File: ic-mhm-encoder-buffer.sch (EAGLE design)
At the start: 35 parts, among them IC1 LS7183-SOIC, J1 2023960907, J2 2023960607, M1 BSS670S2LH6327XTSA1, SW1 CS-4-13NTA, U1 24LC16BT-I/MC, U2 D5V0F4U6S-7, U3 D5V0F4U6S-7, U4 D5V0F4U6S-7

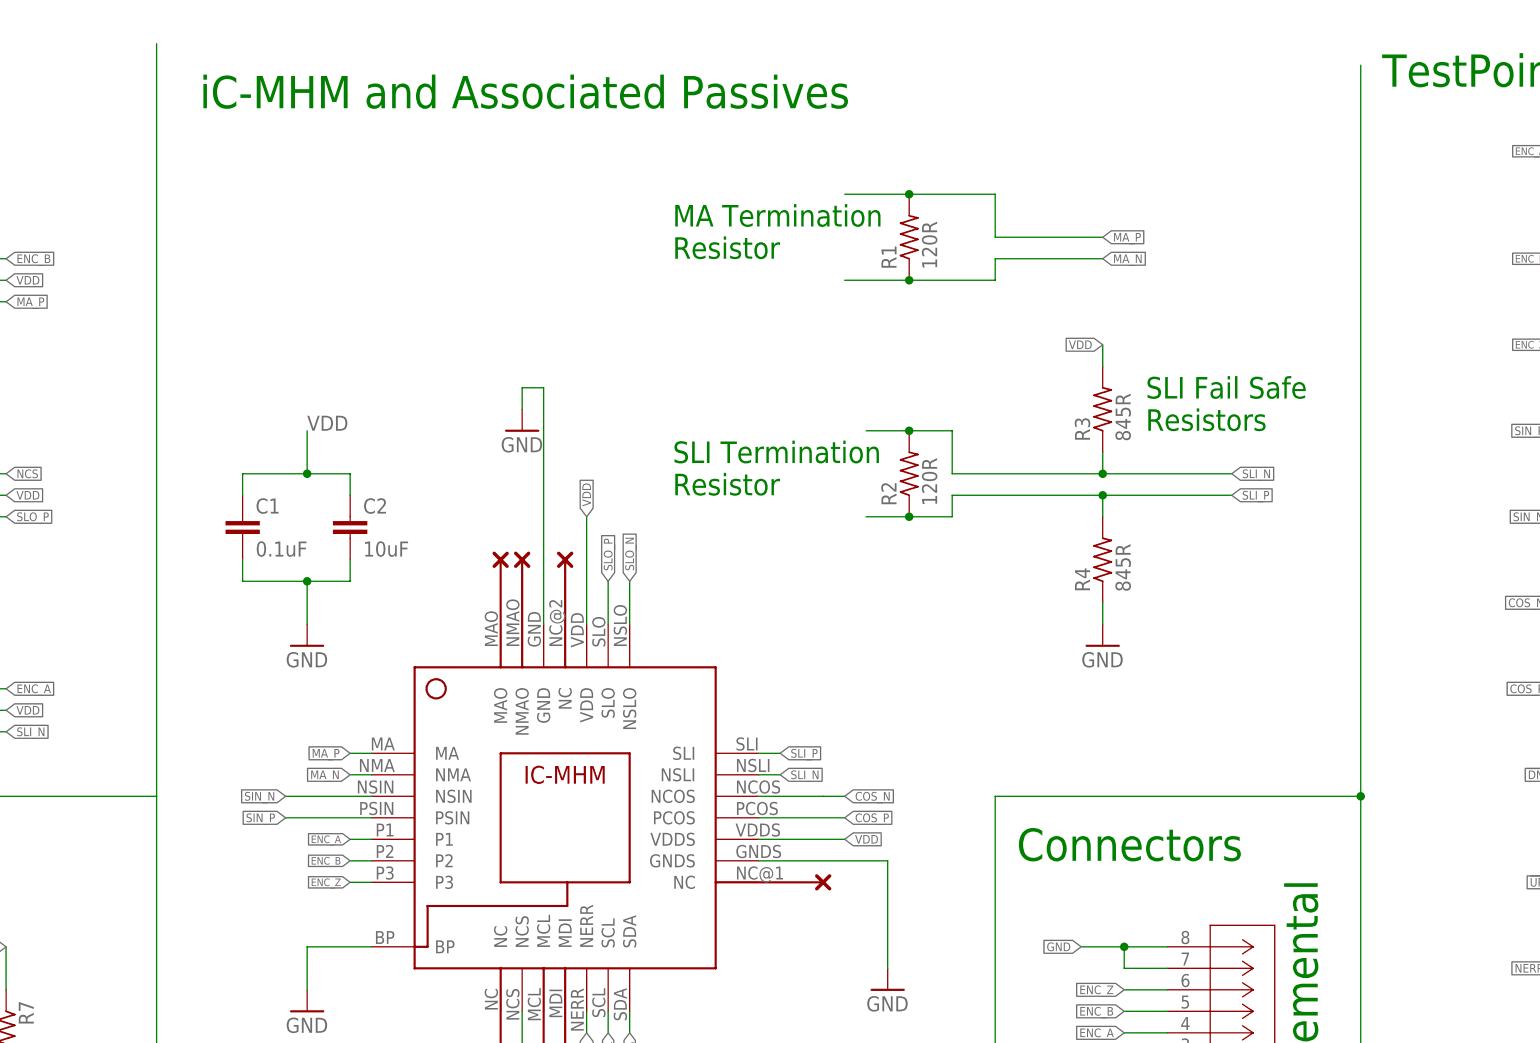
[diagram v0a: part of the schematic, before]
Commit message: added verisons with buffers on ABI
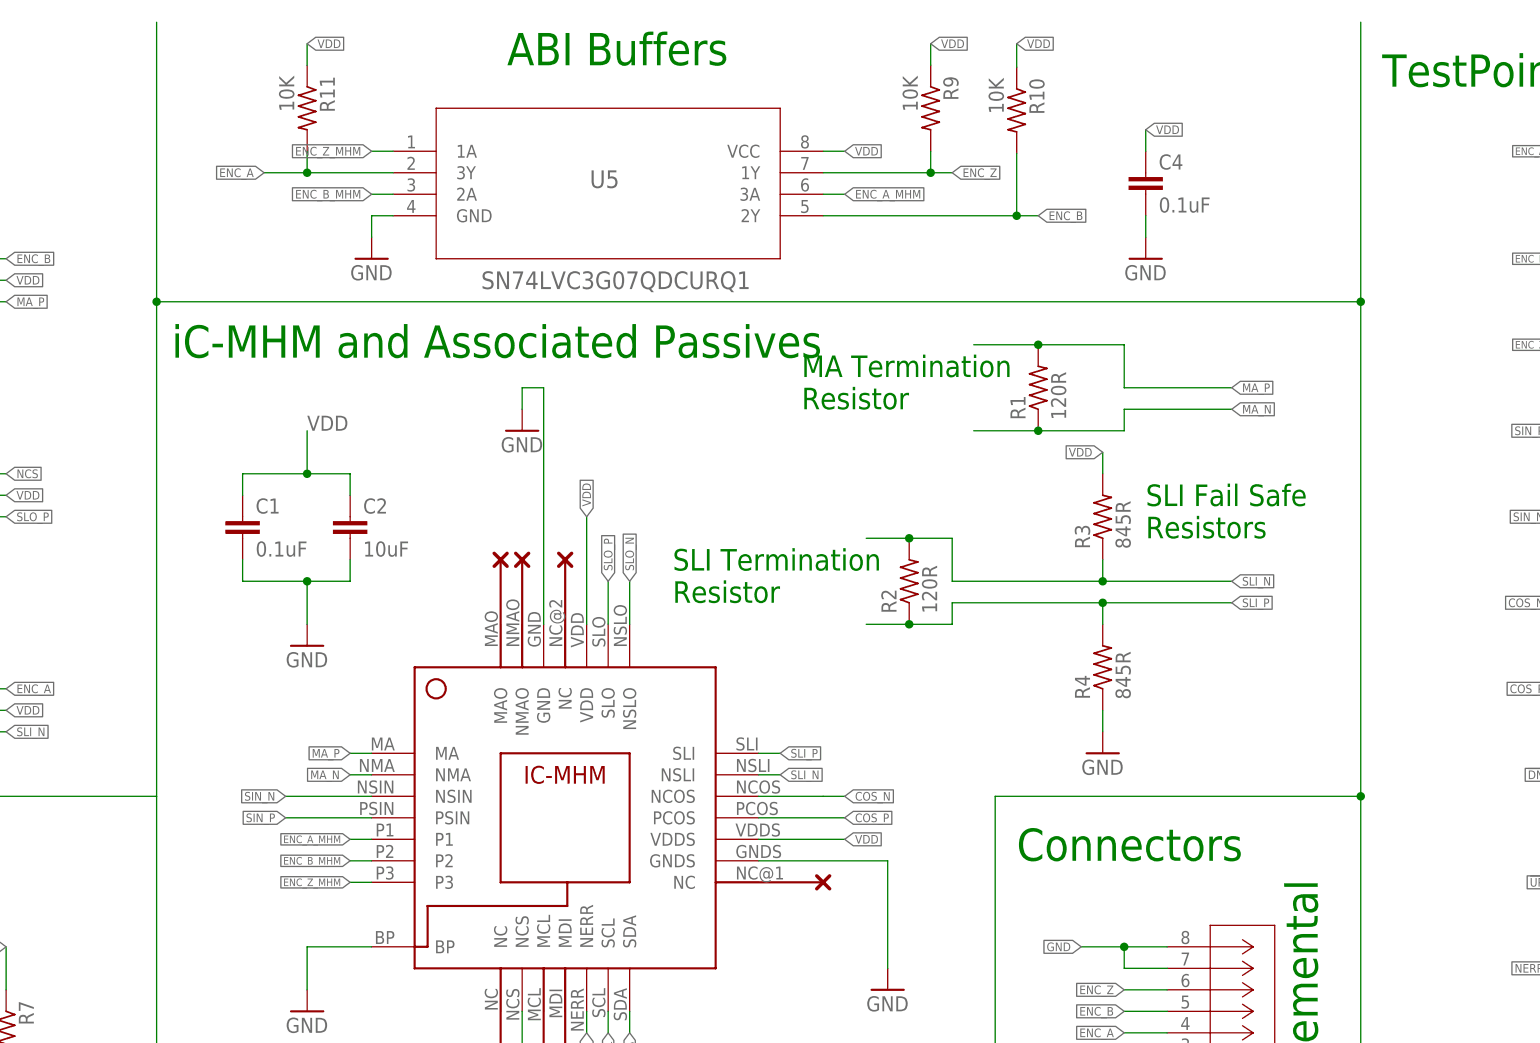
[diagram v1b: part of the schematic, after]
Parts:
- added C4: 0.1uF, rcl:C-EUC0603
- added R10, R11, R9: 10K, rcl:R-US_R0603
- added U5: SN74LVC3G07QDCURQ1, ic-mhm:SN74LVC3G07QDCURQ1
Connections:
- new net ENC_A_MHM: U$1.P1, U5.3A
- new net ENC_B_MHM: U$1.P2, U5.2A
- new net ENC_Z_MHM: U$1.P3, U5.1A
- net ENC_A: now also R11.2, U5.3Y; no longer U$1.P1
- net ENC_B: now also R10.2, U5.2Y; no longer U$1.P2
- net ENC_Z: now also R9.2, U5.1Y; no longer U$1.P3
- net GND: now also C4.2, U5.GND
- net VDD: now also C4.1, R10.1, R11.1, R9.1, U5.VCC
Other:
- note added: "ABI Buffers"
- moved on the sheet: R1, R2, R3, R4
